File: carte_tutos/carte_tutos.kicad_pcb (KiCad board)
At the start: 2 copper layers, 90 parts, among them J1 Conn_01x03_Male, J2 Conn_01x03_Male, J3 Barrel_Jack, J4 Conn_01x04_Male, J5 Conn_01x02_Male, J6 Conn_01x03_Male, J7 Conn_01x02_Male, J8 Conn_01x03_Male, Q1 SFH_3410-Z, SW1 Rotary_Encoder_Switch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

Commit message: More layout, and small schematic edits.
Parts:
- added R9: 100, Resistor_SMD:R_0603_1608Metric_Pad0.98x0.95mm_HandSolder, F.Cu at (95.6, 64.1)
- RV2: footprint Potentiometer_THT:Potentiometer_Bourns_PTA2043_Single_Slide -> Potentiometer_THT:Potentiometer_Bourns_PTV09A-1_Single_Vertical
- moved SW1 315.1 mm to (180.0, 141.7)
- moved J2 269.9 mm to (179.7, 119.0), turned to 270 degrees
- moved J1 267.2 mm to (180.0, 115.1), turned to 270 degrees
- moved J8 264.7 mm to (199.8, 53.7), turned to 180 degrees
- moved J7 263.7 mm to (225.8, 50.0)
- moved R4 254.3 mm to (169.1, 149.6)
- moved R5 254.3 mm to (173.6, 149.6)
- moved R2 240.8 mm to (176.1, 110.2)
- moved C8 237.3 mm to (222.0, 51.3), turned to 270 degrees
- moved D1 236.7 mm to (171.7, 110.2)
- moved R3 227.3 mm to (182.2, 82.8)
- moved D2 226.2 mm to (177.2, 83.3)
- moved J4 225.4 mm to (79.9, 136.8)
- moved RV1 223.7 mm to (93.1, 121.7), turned to 180 degrees
- moved D3 222.3 mm to (92.6, 156.1), turned to 180 degrees
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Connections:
- U3 pad 9: (no net) -> GND
- U4 pad 32: POT -> BUZZ
- U4 pad 34: BUZZ -> POT
- U5 pad 13: INT_TCA -> Net-(R9-Pad1)
- U6 pad 10: /AtLed7 -> /AtLed6
- U6 pad 11: /AtLed8 -> /AtLed4
- U6 pad 12: /AtLed9 -> /AtLed5
- U6 pad 2: /AtLed1 -> /AtLed3
- U6 pad 4: /AtLed3 -> /AtLed1
- U6 pad 5: /AtLed4 -> /AtLed9
- U6 pad 6: /AtLed5 -> /AtLed8
- U6 pad 7: /AtLed6 -> /AtLed7
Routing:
- net Enc2A: track 0.00 -> 110.5 mm, vias 0 -> 1
- net MotA: track 0.00 -> 87.2 mm
- net +3V3: track 0.00 -> 59.5 mm
- net Net-(U1-Pad4): track 0.00 -> 57.9 mm
- net Enc2B: track 0.00 -> 53.7 mm, vias 0 -> 1
- net +12V: track 0.00 -> 53.5 mm
- net Net-(U1-Pad5): track 0.00 -> 47.7 mm
- net Display_DIO: track 0.00 -> 42.7 mm
- net /AtLed4: track 0.00 -> 41.1 mm
- net MotB: track 0.00 -> 40.8 mm
- net Net-(U1-Pad8): track 0.00 -> 39.9 mm, vias 0 -> 1
- net Net-(U1-Pad6): track 0.00 -> 37.2 mm
- net GND: track 0.00 -> 35.5 mm, vias 0 -> 4
- net /AtLed5: track 0.00 -> 33.8 mm
- net Net-(U1-Pad2): track 0.00 -> 33.3 mm, vias 0 -> 1
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- added copper zone on F.Cu, net +3V3

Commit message: Layout almost complete.
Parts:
- added REF**: MountingHole_3.2mm_M3, MountingHole:MountingHole_3.2mm_M3, F.Cu at (73.7, 155.6)
- moved R13 67.5 mm to (89.9, 103.9), turned to 180 degrees
- moved SW2 67.3 mm to (84.8, 99.4), turned to 270 degrees
- moved JP1 65.7 mm to (90.9, 98.1)
- moved JP2 50.2 mm to (90.9, 113.9), turned to 180 degrees
- moved D14 49.2 mm to (179.5, 74.3)
- moved D8 49.2 mm to (189.5, 76.1)
- moved C8 49.2 mm to (193.4, 91.4)
- moved D10 49.2 mm to (189.5, 68.3)
- moved D11 49.2 mm to (186.1, 66.4)
- moved D12 49.2 mm to (182.1, 67.1)
- moved D13 49.2 mm to (179.5, 70.1)
- moved D15 49.2 mm to (182.1, 77.3)
- moved D16 49.2 mm to (186.1, 78.0)
- moved J7 49.2 mm to (197.2, 90.1)
- moved Q1 49.2 mm to (195.3, 100.4)
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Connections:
- U4 pad 37: Attiny_link -> Net-(U4-Pad37)
- U4 pad 54: Net-(U4-Pad54) -> Attiny_link
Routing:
- net +3V3: track 59.5 -> 375.4 mm, vias 0 -> 8
- net +5VP: track 0.00 -> 126.8 mm
- net +5V: track 28.6 -> 154.4 mm, vias 0 -> 3
- net SDA1: track 31.1 -> 120.6 mm, vias 0 -> 1
- net INT_TCA: track 0.00 -> 80.4 mm, vias 0 -> 1
- net SCL1: track 27.7 -> 98.8 mm
- net Enc1B: track 0.00 -> 46.9 mm
- net LED2: track 0.00 -> 46.6 mm
- net SERVO1: track 0.00 -> 42.2 mm
- net Enc1A: track 0.00 -> 40.7 mm
- net Net-(R20-Pad1): track 0.00 -> 29.8 mm
- net SERVO2: track 0.00 -> 29.6 mm
- net LED1: track 0.00 -> 26.7 mm, vias 0 -> 1
- net BTN1: track 0.00 -> 26.0 mm
- net Net-(D3-Pad2): track 0.00 -> 23.7 mm
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- added copper zone on B.Cu, net +3V3
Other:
- board outline added: 133 x 117 mm
- board text added: "GND"
- board text added: "RX"
- board text added: "TX"

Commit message: Finish layout.
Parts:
- removed the REF** at (73.7, 155.6)
- added REF**: KiCad-Logo2_5mm_SilkScreen, Symbol:KiCad-Logo2_5mm_SilkScreen, B.Cu at (183.6, 48.8)
- added REF**: Polarity_Center_Positive_6mm_SilkScreen, Symbol:Polarity_Center_Positive_6mm_SilkScreen, F.Cu at (73.7, 119.0)
- added REF**: MountingHole_3.2mm_M3, MountingHole:MountingHole_3.2mm_M3, F.Cu at (75.0, 49.0)
- added REF**: MountingHole_3.2mm_M3, MountingHole:MountingHole_3.2mm_M3, F.Cu at (196.0, 49.0)
- added REF**: MountingHole_3.2mm_M3, MountingHole:MountingHole_3.2mm_M3, F.Cu at (196.0, 154.0)
- added REF**: MountingHole_3.2mm_M3, MountingHole:MountingHole_3.2mm_M3, F.Cu at (75.0, 154.0)
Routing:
- net +3V3: track 375.4 -> 402.2 mm, vias 8 -> 10
- net GND: track 39.9 -> 65.3 mm, vias 7 -> 19
- net +5V: track 154.4 -> 159.7 mm
- added copper zone on B.Cu, net GND
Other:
- outline, holes or cut-outs redrawn
- board text added: "UART"

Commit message: silk
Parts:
- moved D6 1.91 mm to (87.0, 70.5)
- moved D7 1.91 mm to (88.9, 70.5)
- moved R27 1.91 mm to (87.0, 75.0)
- moved R37 1.91 mm to (88.9, 75.0)
- moved J6 0.38 mm to (86.4, 48.0)
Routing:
- net +3V3: track 402.2 -> 396.4 mm
- net Net-(D7-Pad1): track 4.56 -> 6.39 mm
- net Net-(D6-Pad1): track 6.11 -> 7.25 mm
- net GND: track 65.3 -> 66.2 mm
- net SDA1: track 120.6 -> 119.7 mm
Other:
- board text added: "B1"
- board text added: "B2"
- board text added: "B3"
- board text added: "B4"
- board text added: "Encoder"
- board text added: "I2C"
- board text added: "Motor"
- board text added: "Pot1"
- board text added: "Pot2"
- board text added: "SCL"
- board text added: "SDA"
- board text added: "Servo1"
- board text added: "Servo2"

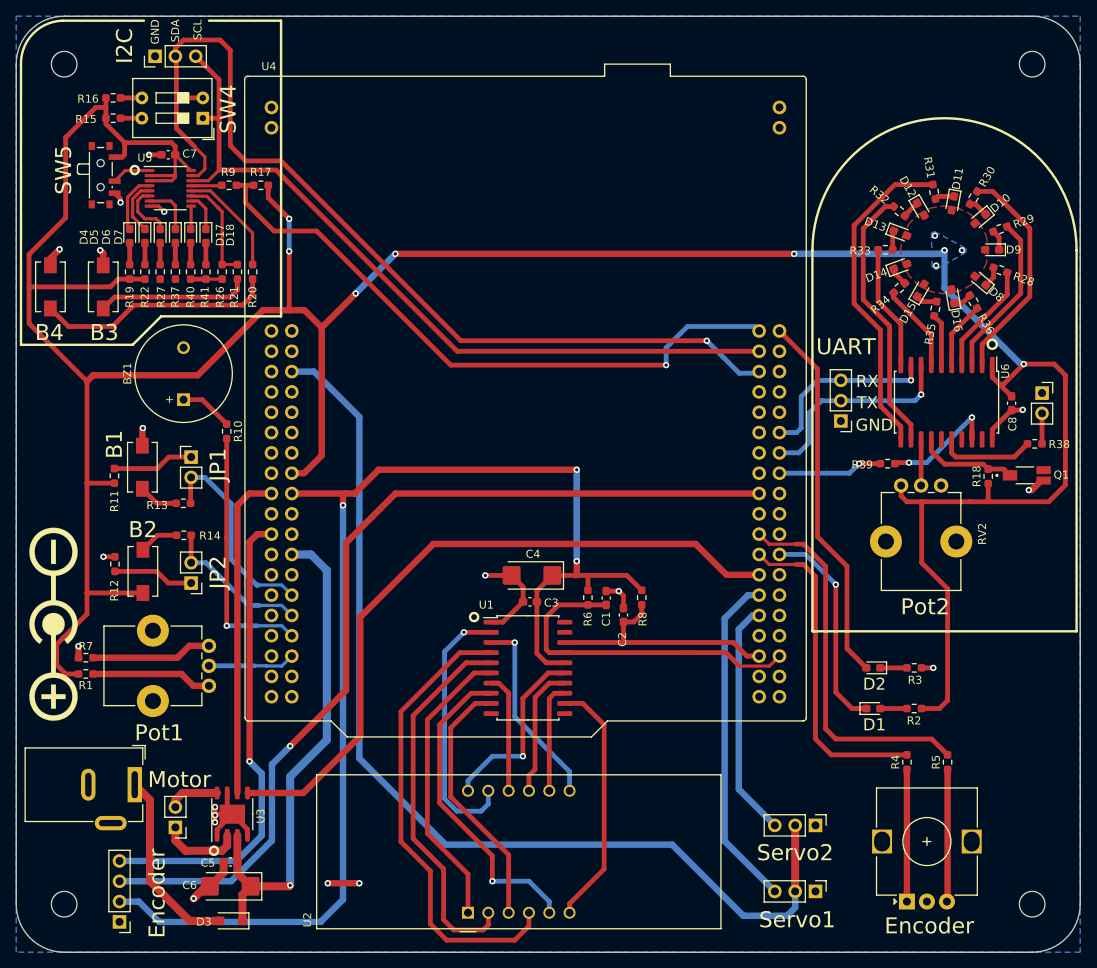
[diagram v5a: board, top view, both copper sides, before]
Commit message: More silk, and add power led.
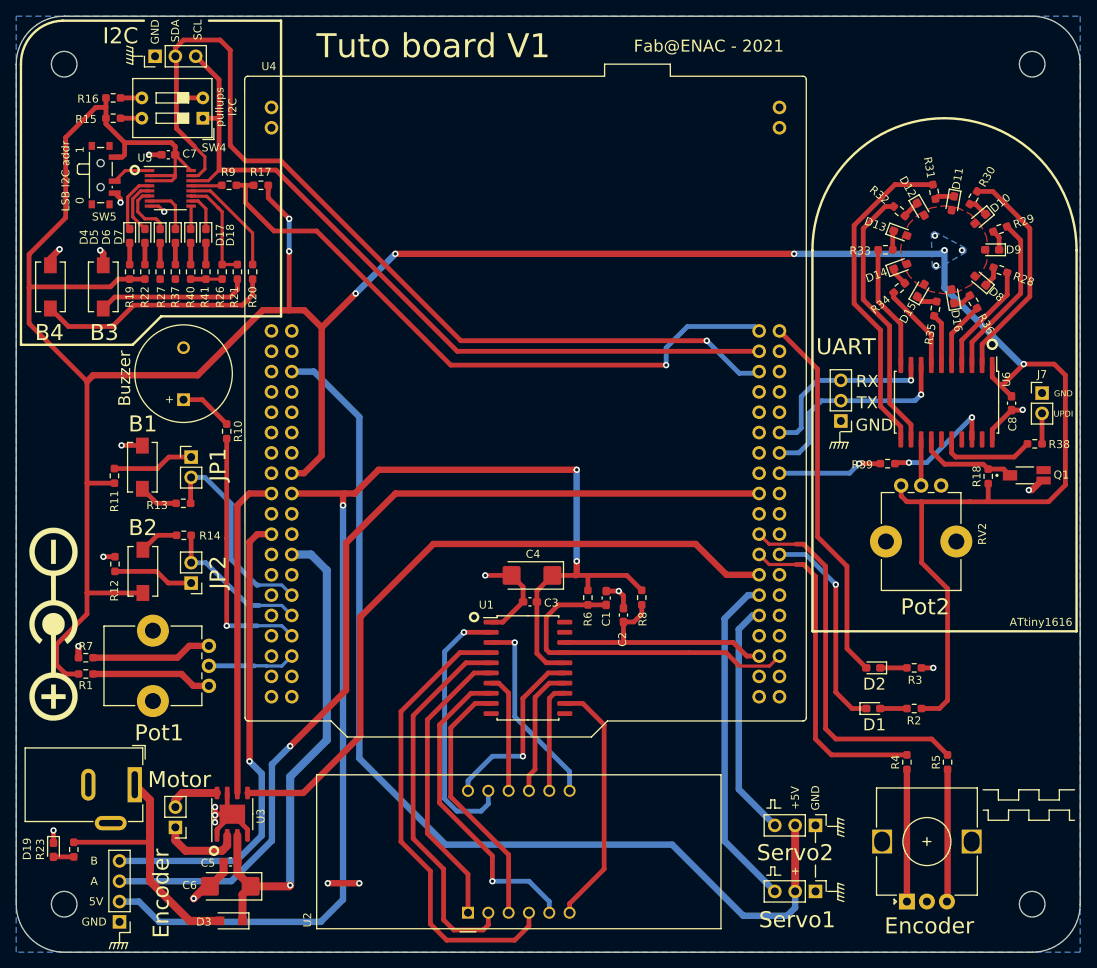
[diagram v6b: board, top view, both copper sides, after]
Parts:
- added D19: LED, LED_SMD:LED_0603_1608Metric_Pad1.05x0.95mm_HandSolder, F.Cu at (73.7, 147.2)
- added R23: 2k, Resistor_SMD:R_0603_1608Metric_Pad0.98x0.95mm_HandSolder, F.Cu at (76.2, 147.2)
- J7: footprint Connector_PinSocket_2.54mm:PinSocket_1x02_P2.54mm_Vertical -> Connector_PinHeader_2.54mm:PinHeader_1x02_P2.54mm_Vertical
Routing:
- net Net-(D3-Pad2): track 23.7 -> 33.4 mm
- net Net-(D19-Pad2): track 0.00 -> 2.54 mm
- net GND: track 66.2 -> 68.1 mm, vias 19 -> 20
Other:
- board text added: "+"
- board text added: "+5V"
- board text added: "0"
- board text added: "1"
- board text added: "5V"
- board text added: "A"
- board text added: "ATtiny1616"
- board text added: "B"
- board text added: "Buzzer"
- board text added: "Fab@ENAC - 2021"
- board text added: "LSB I2C addr"
- board text added: "Tuto board V1"
- board text added: "UPDI"
- board text added: "pullups I2C"

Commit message: Improve Silk.
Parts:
- removed the REF** at (73.7, 119.0)
- added REF**: Symbol_Barrel_Polarity, Symbol:Symbol_Barrel_Polarity, F.Cu at (74.8, 132.0)
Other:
- board text added: "-"
- board text added: "12V"
- board text added: "NUCLEO-F401RE NUCLEO-F411RE NUCLEO-F410RB"
- board text added: "POWER"

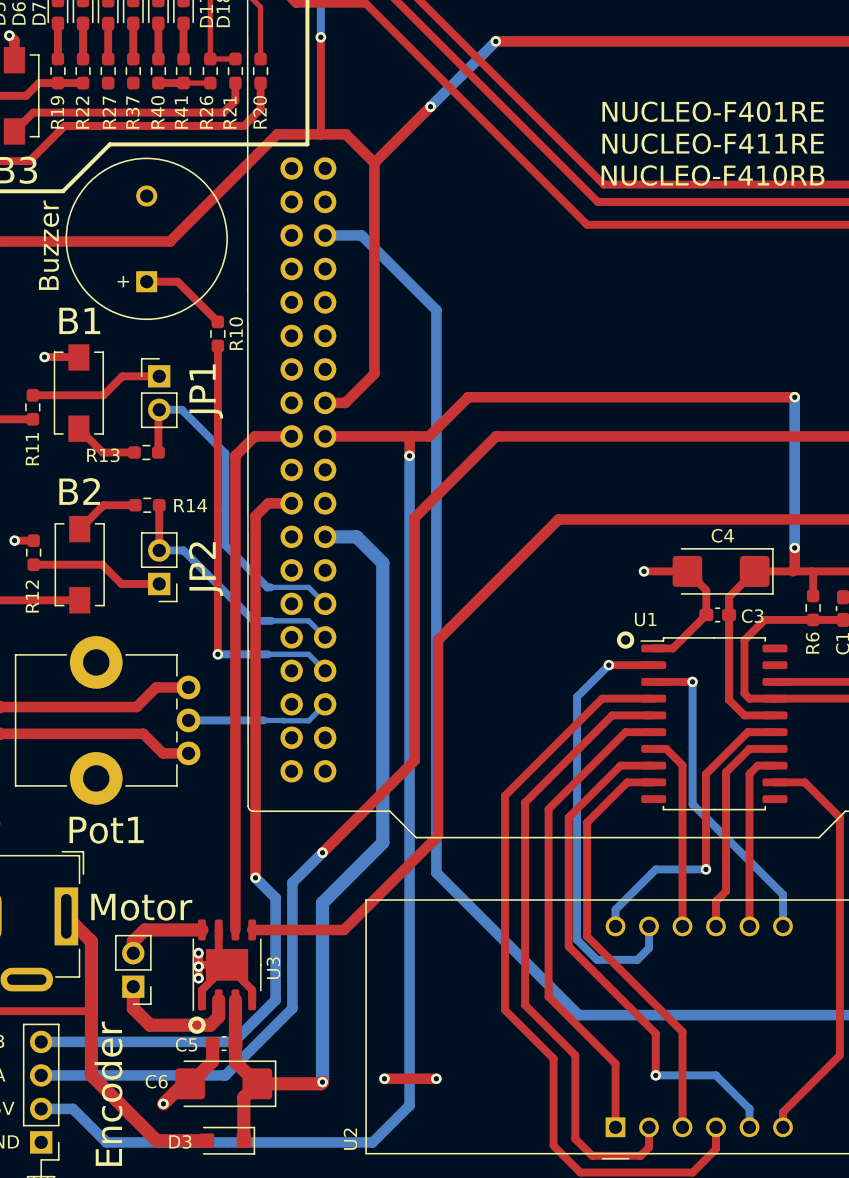
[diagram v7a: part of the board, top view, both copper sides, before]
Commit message: Fix unrouted track.
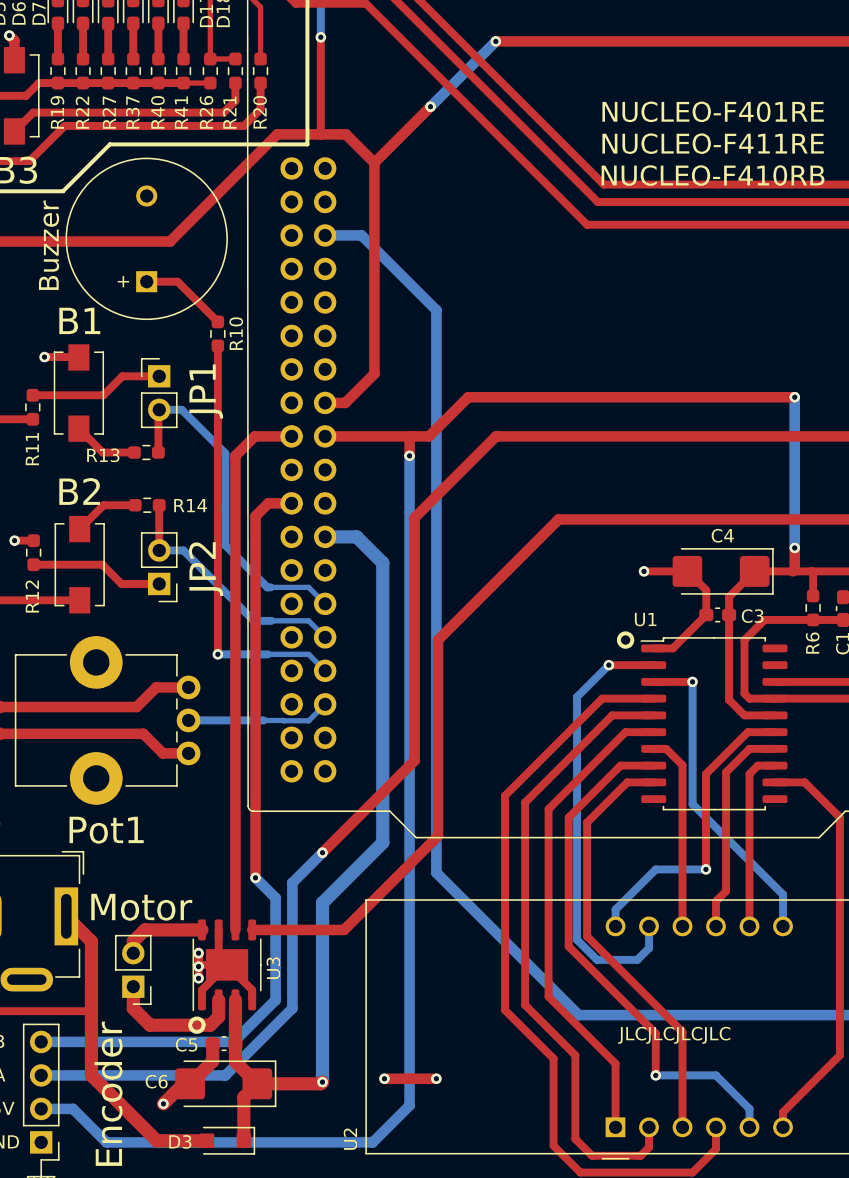
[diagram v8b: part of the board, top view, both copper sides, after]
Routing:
- net +3V3: track 396.4 -> 402.2 mm
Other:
- board text added: "JLCJLCJLCJLC"
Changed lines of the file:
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@@
   (general
     (thickness 1.6)
-    (drawings 132)
-    (tracks 638)
+    (drawings 133)
+    (tracks 641)
     (zones 0)
     (modules 99)
@@
     (pcbplotparams
       (layerselection 0x010fc_ffffffff)
-      (usegerberextensions false)
-      (usegerberattributes true)
-      (usegerberadvancedattributes true)
-      (creategerberjobfile true)
+      (usegerberextensions true)
+      (usegerberattributes false)
+      (usegerberadvancedattributes false)
+      (creategerberjobfile false)
       (excludeedgelayer true)
       (linewidth 0.100000)
@@
       (psa4output false)
       (plotreference true)
-      (plotvalue true)
+      (plotvalue false)
       (plotinvisibletext false)
       (padsonsilk false)
-      (subtractmaskfromsilk false)
+      (subtractmaskfromsilk true)
       (outputformat 1)
       (mirror false)
-      (drillshape 1)
+      (drillshape 0)
       (scaleselection 1)
-      (outputdirectory ""))
+      (outputdirectory "gerbers/"))
   )
   (net 0 "")
@@
       (effects (font (size 1 1) (thickness 0.15)))
     )
-    (fp_arc (start 0 0.075) (end 0.75 0.75) (angle 270) (layer F.SilkS) (width 0.15))
     (fp_line (start 0 0.075) (end 2 0.075) (layer F.SilkS) (width 0.15))
     (fp_line (start -2 0.075) (end -1.1 0.075) (layer F.SilkS) (width 0.15))
@@
     (fp_circle (center 3 0.075) (end 3 1) (layer F.SilkS) (width 0.15))
     (fp_circle (center 0 0.075) (end 0 0.25) (layer F.SilkS) (width 0.5))
+    (fp_arc (start 0 0.075) (end 0.75 0.75) (angle 270) (layer F.SilkS) (width 0.15))
   )
   (module Resistor_SMD:R_0603_1608Metric_Pad0.98x0.95mm_HandSolder (layer F.Cu)
@@
       (effects (font (size 1 1) (thickness 0.15)))
     )
-    (pad 2 smd roundrect (at 2.55 0 180) (size 2.25 2.35) (layers F.Cu F.Paste F.Mask) (roundrect_rratio 0.111111)
+    (pad 2 smd roundrect (at 2.55 0 180) (size 2.25 2.35) (layers F.Cu F.Paste F.Mask) (roundrect_rratio 0.1111106666666667)
       (net 1 GND))
-    (pad 1 smd roundrect (at -2.55 0 180) (size 2.25 2.35) (layers F.Cu F.Paste F.Mask) (roundrect_rratio 0.111111)
+    (pad 1 smd roundrect (at -2.55 0 180) (size 2.25 2.35) (layers F.Cu F.Paste F.Mask) (roundrect_rratio 0.1111106666666667)
       (net 6 +12V))
     (model ${KISYS3DMOD}/Capacitor_Tantalum_SMD.3dshapes/CP_EIA-6032-28_Kemet-C.wrl
@@
       (effects (font (size 1 1) (thickness 0.15)))
     )
-    (pad 2 smd roundrect (at 2.55 0 180) (size 2.25 2.35) (layers F.Cu F.Paste F.Mask) (roundrect_rratio 0.111111)
+    (pad 2 smd roundrect (at 2.55 0 180) (size 2.25 2.35) (layers F.Cu F.Paste F.Mask) (roundrect_rratio 0.1111106666666667)
       (net 1 GND))
-    (pad 1 smd roundrect (at -2.55 0 180) (size 2.25 2.35) (layers F.Cu F.Paste F.Mask) (roundrect_rratio 0.111111)
+    (pad 1 smd roundrect (at -2.55 0 180) (size 2.25 2.35) (layers F.Cu F.Paste F.Mask) (roundrect_rratio 0.1111106666666667)
       (net 5 +5V))
     (model ${KISYS3DMOD}/Capacitor_Tantalum_SMD.3dshapes/CP_EIA-6032-28_Kemet-C.wrl
@@
     )
   )
+  (gr_text JLCJLCJLCJLC (at 130 148) (layer F.SilkS)
+    (effects (font (size 1 1) (thickness 0.15)))
+  )
   (gr_text "NUCLEO-F401RE\nNUCLEO-F411RE\nNUCLEO-F410RB" (at 132.842 80.518) (layer F.SilkS)
     (effects (font (size 1.5 1.5) (thickness 0.3)))
@@
   (segment (start 103.124 79.756) (end 99.822 79.756) (width 0.8) (layer F.Cu) (net 7))
   (segment (start 105.029 79.756) (end 103.124 79.756) (width 0.8) (layer F.Cu) (net 7))
+  (segment (start 86.995 75.866) (end 85.09 75.866) (width 0.6) (layer F.Cu) (net 7))
+  (segment (start 86.995 75.866) (end 88.9 75.866) (width 0.6) (layer F.Cu) (net 7))
+  (segment (start 88.9 75.866) (end 90.805 75.866) (width 0.6) (layer F.Cu) (net 7))
   (segment (start 177.01 129.54) (end 180.34 129.54) (width 0.6) (layer F.Cu) (net 8))
   (segment (start 164.41 110.285) (end 167.689 110.285) (width 0.6) (layer B.Cu) (net 9))
